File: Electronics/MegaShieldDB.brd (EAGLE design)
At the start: 100.3 x 80 mm, 45 parts, among them IC2 MCP4802, IC3 MCP4802, IC4 4013N, Q1 BF199, Q5 BF199, X1 Panel, X2 Cruise, X3 Motor, X4 Steer, X5 Brake

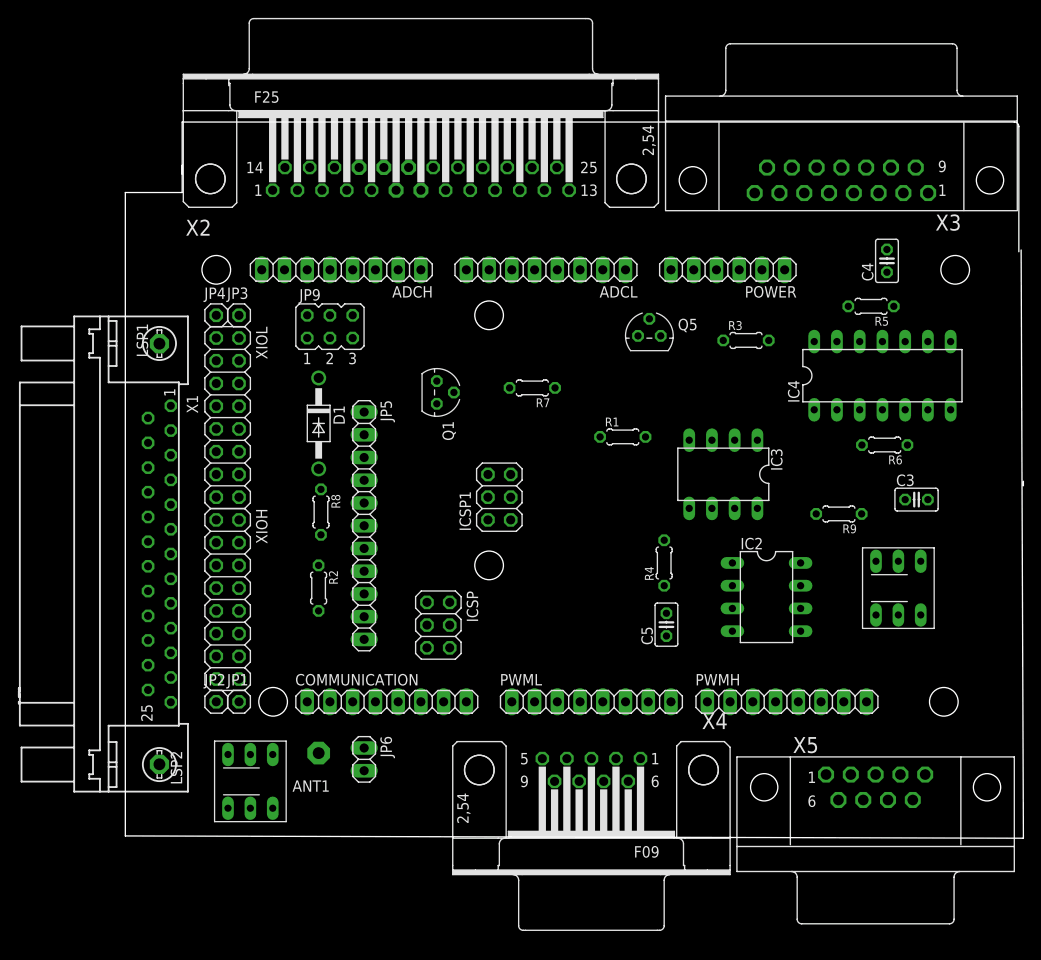
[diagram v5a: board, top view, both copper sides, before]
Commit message: Routed with thick power and ground.
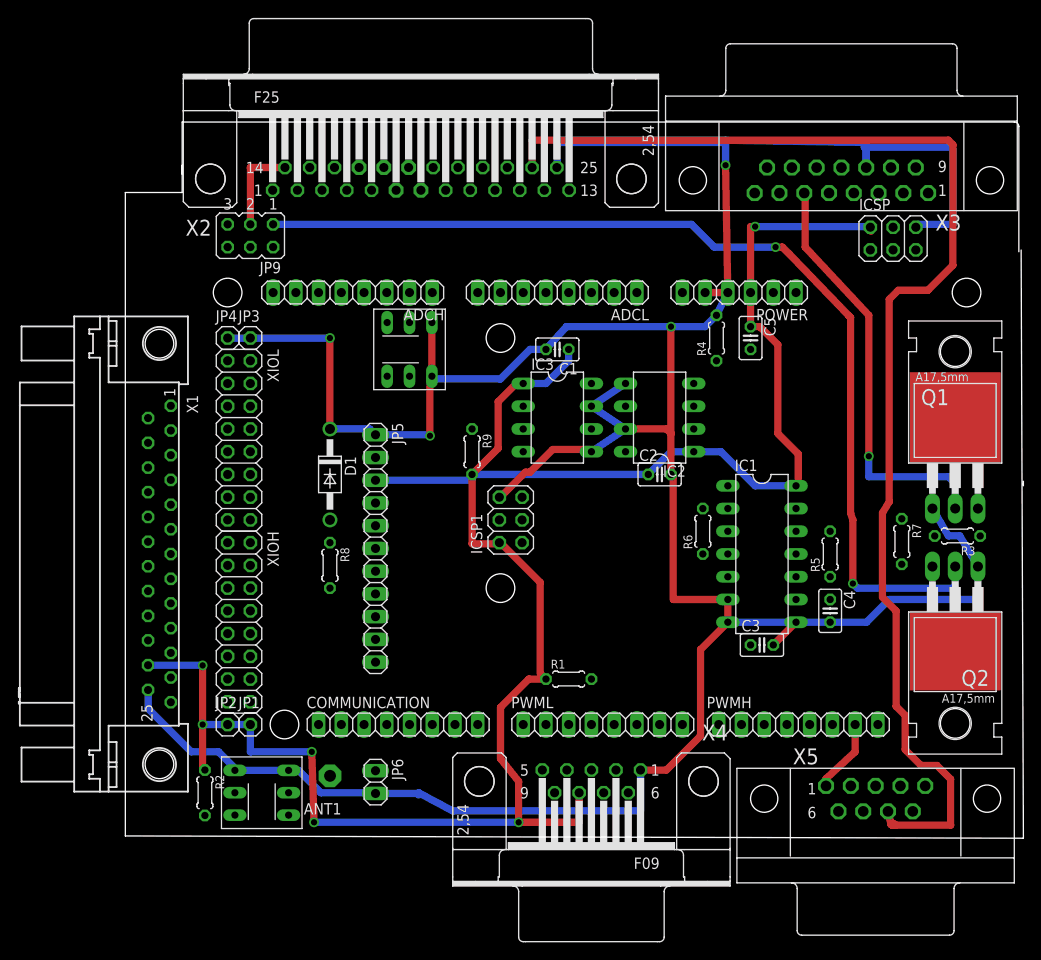
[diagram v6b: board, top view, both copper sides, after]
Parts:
- removed IC4: 4013N, ic-package:DIL14
- removed LSP1, LSP2: LSP13, solpad:LSP13
- removed Q5: BF199, transistor-npn:TO92
- added C1, C2: 0.1uF, rcl:C025-025X050
- added IC1: 4013N, ic-package:DIL14
- added Q2: TIP3055, transistor-neu-to92:TO220
- JP9: value (none) -> Wireless Select
- Q1: value BF199 -> TIP3055; device transistor-npn:TO92 -> transistor-neu-to92:TO220
- R3, R7: value 4.7k -> 1.5k
- moved ICSP 66.7 mm to (85.8, 67.0), turned to 0 degrees
- moved U$2 60.8 mm to (31.8, 54.6)
- moved Q1 58.3 mm to (92.7, 43.2), turned to 0 degrees
- moved R7 44.7 mm to (86.7, 33.1), turned to 270 degrees
- moved R9 41.6 mm to (38.7, 43.2), turned to 270 degrees
- moved C4 39.6 mm to (78.7, 25.4), turned to 270 degrees
- moved C5 33.4 mm to (69.8, 55.9), turned to 270 degrees
- moved R3 32.2 mm to (93.0, 33.8), turned to 180 degrees
- moved R5 28.0 mm to (78.7, 31.8), turned to 90 degrees
- moved R1 27.7 mm to (49.5, 17.8)
- moved R2 26.2 mm to (8.89, 5.08)
- moved R4 25.8 mm to (66.0, 55.9)
- moved C3 23.7 mm to (71.1, 21.6)
- moved IC2 23.3 mm to (59.7, 47.0), turned to 90 degrees
- moved R6 22.5 mm to (64.5, 34.3), turned to 90 degrees
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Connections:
- removed net N$12: Q1.1, R7.2
- new net N$3: Q2.3, R7.2
- net +5V: now also C1.1, C2.1, IC1.14; no longer IC4.14
- net CLKA: now also IC1.3, JP9.2; no longer IC4.3, JP9.6
- net CLKB: now also IC1.11; no longer IC4.11
- net D0RX0: now also JP9.5; no longer JP9.1
- net D3INT1: now also JP9.6; no longer JP9.2
- net DA: now also IC1.5; no longer IC4.5
- net DB: now also IC1.9; no longer IC4.9
- net GND: now also C1.2, C2.2, IC1.6, IC1.7, IC1.8, Q1.1, Q2.1; no longer IC4.6, IC4.7, IC4.8, Q1.2, Q5.2
- net N$2: now also IC1.1; no longer IC4.1
- net N$33: now also Q1.3; no longer Q5.1
- net N$4: now also IC1.13; no longer IC4.13
- net N$7: now also IC1.2; no longer IC4.2
- net RA: now also IC1.10, IC1.4; no longer IC4.10, IC4.4
- net WLES: now also Q1.2; no longer Q5.3
- net WLXCOLL: now also JP9.1, Q2.2; no longer JP9.5, Q1.3
- net ~QB: now also IC1.12; no longer IC4.12
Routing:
- net GND: track 0.00 -> 403.6 mm, vias 0 -> 4
- net +5V: track 0.00 -> 238.3 mm, vias 0 -> 6
- net 5VBRK: track 0.00 -> 144.8 mm
- net WLXCOLL: track 0.00 -> 112.8 mm, vias 0 -> 2
- net WLES: track 0.00 -> 47.3 mm, vias 0 -> 1
- net X2-14: track 0.00 -> 10.2 mm

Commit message: New documentation of PCB board; added notes on signals;PCB board layout as built.
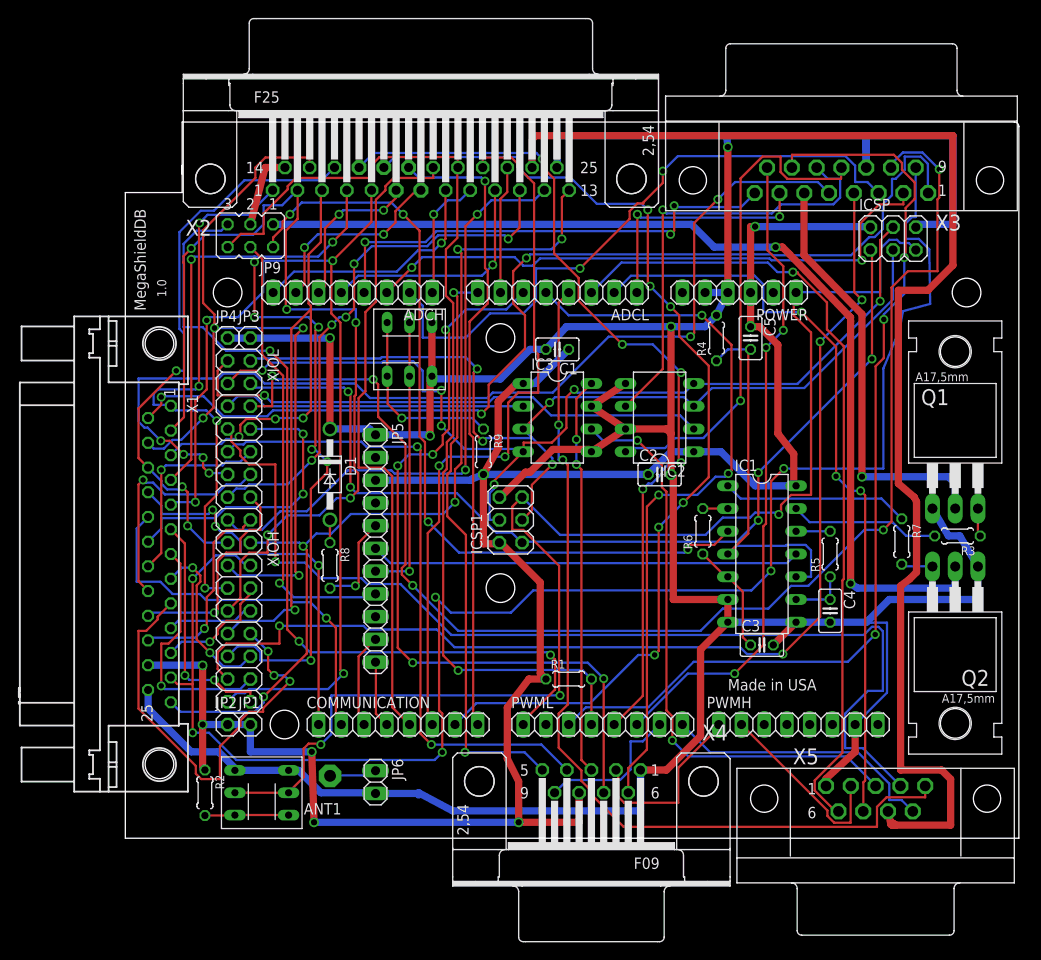
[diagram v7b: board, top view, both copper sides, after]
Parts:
- moved R9 1.27 mm to (40.0, 43.2)
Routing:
- net D34: track 0.00 -> 177.4 mm, vias 0 -> 6
- net D48: track 0.00 -> 153.7 mm, vias 0 -> 5
- net RESET: track 0.00 -> 150.1 mm, vias 0 -> 3
- net D25: track 0.00 -> 125.8 mm, vias 0 -> 4
- net FUEL: track 0.00 -> 117.5 mm, vias 0 -> 3
- net D47: track 0.00 -> 114.3 mm, vias 0 -> 1
- net D43: track 0.00 -> 114.1 mm, vias 0 -> 6
- net D15RXD3: track 0.00 -> 113.6 mm, vias 0 -> 6
- net D23: track 0.00 -> 113.3 mm, vias 0 -> 4
- net D27: track 0.00 -> 113.2 mm, vias 0 -> 8
- net D3INT1: track 0.00 -> 112.2 mm, vias 0 -> 1
- net D51: track 0.00 -> 110.9 mm, vias 0 -> 6
- net D2INT0: track 0.00 -> 107.6 mm, vias 0 -> 3
- net D52: track 0.00 -> 106.9 mm, vias 0 -> 4
- net N$9: track 0.00 -> 106.8 mm, vias 0 -> 5
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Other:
- board size 100.3 x 80 mm -> 99.8 x 80 mm
- board text added: "1.0"
- board text added: "Made in USA"
- board text added: "MegaShieldDB"

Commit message: 3 new boards
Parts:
- removed R9: 10M, rcl:0204/5
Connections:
- removed net N$10: R9.1, U$2.PIN1, U$2.PIN4
- net +5V: now also U$2.PIN1, U$2.PIN4; no longer R9.2
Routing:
- net +5V: track 234.3 -> 203.5 mm
- net N$10: track 21.0 -> 0.00 mm, vias 1 -> 0
- net N$28: track 31.6 -> 25.6 mm
- net GND: track 401.4 -> 395.4 mm
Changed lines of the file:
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@@
 <element name="R1" library="rcl" package="0204/5" value="1M" x="49.53" y="17.78"/>
 <element name="R2" library="rcl" package="0204/5" value="10M" x="8.89" y="5.08" rot="R270"/>
-<element name="R9" library="rcl" package="0204/5" value="10M" x="40.005" y="43.18" rot="R270"/>
 <element name="X3" library="con-subd" package="182-015-MALE" value="Motor" x="80" y="83" rot="R180">
 <attribute name="OC_NEWARK" value="unknown" x="80" y="83" size="1.778" layer="27" rot="R180" display="off"/>
@@
 <contactref element="R1" pad="1"/>
 <contactref element="R2" pad="1"/>
-<contactref element="R9" pad="2"/>
 <contactref element="C1" pad="1"/>
 <contactref element="C2" pad="1"/>
 <wire x1="8.636" y1="12.7" x2="11.43" y2="12.7" width="0.8128" layer="16"/>
 <wire x1="11.43" y1="12.7" x2="13.97" y2="12.7" width="0.8128" layer="16"/>
-<wire x1="40.005" y1="40.64" x2="58.42" y2="40.64" width="0.8128" layer="16"/>
-<wire x1="40.005" y1="40.64" x2="40.005" y2="32.893" width="0.8128" layer="1"/>
 <wire x1="40.005" y1="32.893" x2="41.783" y2="32.893" width="0.8128" layer="1"/>
 <wire x1="41.783" y1="32.893" x2="41.783" y2="33.02" width="0.8128" layer="1"/>
@@
 <wire x1="27.95" y1="39.99" x2="38.593" y2="39.99" width="0.8128" layer="16"/>
 <wire x1="38.593" y1="39.99" x2="38.735" y2="40.132" width="0.8128" layer="16"/>
-<wire x1="38.735" y1="40.132" x2="40.005" y2="40.64" width="0.8128" layer="16"/>
 <wire x1="2.54" y1="19.3294" x2="8.6106" y2="19.3294" width="0.8128" layer="16"/>
 <wire x1="8.6106" y1="19.3294" x2="8.636" y2="19.304" width="0.8128" layer="16"/>
@@
 <wire x1="43.688" y1="50.8" x2="41.656" y2="48.768" width="0.8128" layer="1"/>
 <wire x1="41.656" y1="48.768" x2="41.656" y2="43.561" width="0.8128" layer="1"/>
-<wire x1="41.656" y1="43.561" x2="40.005" y2="40.64" width="0.8128" layer="1"/>
 <wire x1="83.23" y1="67.9" x2="83.312" y2="67.818" width="0.8128" layer="1"/>
 <wire x1="83.312" y1="68.326" x2="83.2612" y2="68.326" width="0.8128" layer="16"/>
@@
 <wire x1="83.2612" y1="68.2752" x2="83.23" y2="68.26" width="0.254" layer="16"/>
 <wire x1="83.2612" y1="68.2752" x2="83.2612" y2="68.326" width="0.254" layer="16"/>
+<contactref element="U$2" pad="PIN1"/>
+<contactref element="U$2" pad="PIN4"/>
+<wire x1="29.2608" y1="51.6128" x2="29.25" y2="51.61" width="0.254" layer="1"/>
+<wire x1="29.2608" y1="57.6072" x2="29.25" y2="57.61" width="0.254" layer="1"/>
+<wire x1="29.3116" y1="51.5112" x2="29.25" y2="51.61" width="0.254" layer="1"/>
+<wire x1="49.53" y1="54.61" x2="60.96" y2="43.18" width="0" layer="19" extent="16-16"/>
+<wire x1="38.735" y1="40.132" x2="41.656" y2="43.561" width="0" layer="19" extent="1-16"/>
+<wire x1="40.005" y1="32.893" x2="38.593" y2="39.99" width="0" layer="19" extent="1-16"/>
+<wire x1="29.3116" y1="51.5112" x2="27.95" y2="39.99" width="0" layer="19" extent="1-1"/>
+<wire x1="29.25" y1="57.61" x2="29.25" y2="51.61" width="0" layer="19" extent="1-1"/>
 </signal>
 <signal name="GND">
@@
 <contactref element="IC2" pad="5"/>
 <contactref element="C2" pad="2"/>
-<wire x1="34.25" y1="57.61" x2="34.25" y2="51.61" width="0.8128" layer="1"/>
+<wire x1="34.25" y1="57.61" x2="34.25" y2="51.61" width="0" layer="19" extent="1-16"/>
 <wire x1="22.86" y1="45.72" x2="22.86" y2="55.88" width="0.8128" layer="1"/>
 <via x="22.86" y="55.88" extent="1-16" drill="0.7"/>
@@
 <contactref element="U$2" pad="PIN2"/>
 <contactref element="U$2" pad="PIN5"/>
-<wire x1="31.75" y1="57.61" x2="31.75" y2="51.61" width="0.254" layer="1"/>
+<wire x1="31.75" y1="57.61" x2="31.75" y2="51.61" width="0" layer="19" extent="1-16"/>
 <wire x1="31.75" y1="29.8196" x2="27.9908" y2="29.8196" width="0.254" layer="16"/>
 <wire x1="31.75" y1="51.61" x2="31.75" y2="29.8196" width="0.254" layer="1"/>
@@
 <wire x1="12.3444" y1="2.5908" x2="12.24" y2="2.58" width="0.254" layer="1"/>
 </signal>
-<signal name="N$10">
-<contactref element="R9" pad="1"/>
-<contactref element="U$2" pad="PIN1"/>
-<contactref element="U$2" pad="PIN4"/>
-<wire x1="29.2608" y1="57.6072" x2="29.2608" y2="51.6128" width="0.254" layer="1"/>
-<wire x1="29.2608" y1="51.6128" x2="29.25" y2="51.61" width="0.254" layer="1"/>
-<wire x1="29.2608" y1="57.6072" x2="29.25" y2="57.61" width="0.254" layer="1"/>
-<wire x1="38.7604" y1="46.9392" x2="39.9796" y2="45.72" width="0.254" layer="16"/>
-<wire x1="30.8864" y1="46.9392" x2="38.7604" y2="46.9392" width="0.254" layer="16"/>
-<wire x1="29.3116" y1="48.514" x2="30.8864" y2="46.9392" width="0.254" layer="1"/>
-<wire x1="29.3116" y1="51.5112" x2="29.3116" y2="48.514" width="0.254" layer="1"/>
-<wire x1="39.9796" y1="45.72" x2="40.005" y2="45.72" width="0.254" layer="16"/>
-<wire x1="29.3116" y1="51.5112" x2="29.25" y2="51.61" width="0.254" layer="1"/>
-<via x="30.8864" y="46.9392" extent="1-16" drill="0.6096"/>
-</signal>
 <signal name="D3INT1">
